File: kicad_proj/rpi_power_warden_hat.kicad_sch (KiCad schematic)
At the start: 4 parts, among them J1 54-00164, J2 54-00164, J3 54-00003

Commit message: checked all the schematics
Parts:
- TP1: now left out of the parts list
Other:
- moved on the sheet: J1, J2, J3, TP1

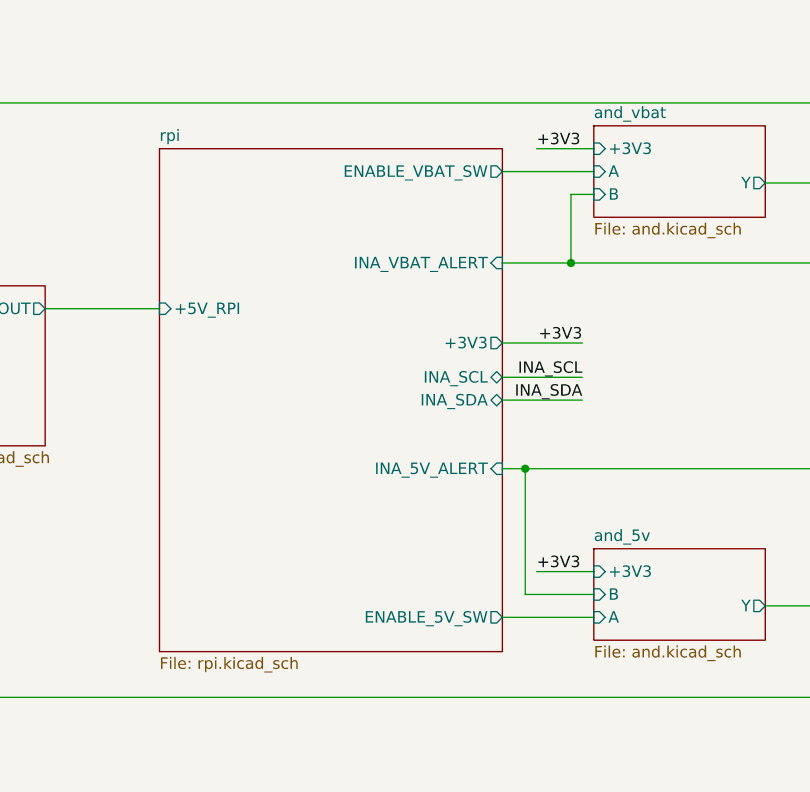
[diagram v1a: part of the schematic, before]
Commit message: run ERC and fix some errors (no critical errors, mostly associated to raspberry pi connectors not connected and with not NC flag
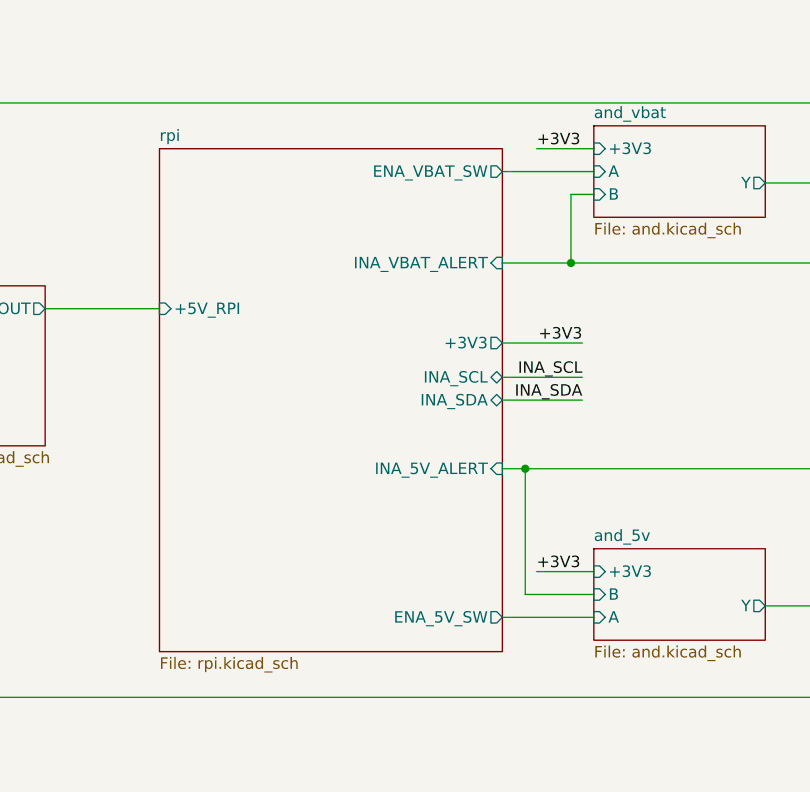
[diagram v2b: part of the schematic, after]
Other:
- sheet rpi ports: added ENA_5V_SW, ENA_VBAT_SW; removed ENABLE_5V_SW, ENABLE_VBAT_SW
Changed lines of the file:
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@@
 			)
 		)
-		(pin "ENABLE_5V_SW" output
+		(pin "ENA_5V_SW" output
 			(at 130.81 115.57 0)
 			(effects
@@
 			)
 		)
-		(pin "ENABLE_VBAT_SW" output
+		(pin "ENA_VBAT_SW" output
 			(at 130.81 66.04 0)
 			(effects

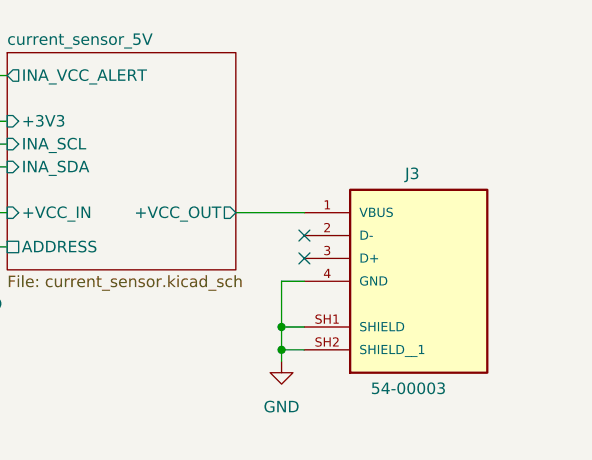
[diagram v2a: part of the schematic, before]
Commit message: changed usb A for an usb C with more stock
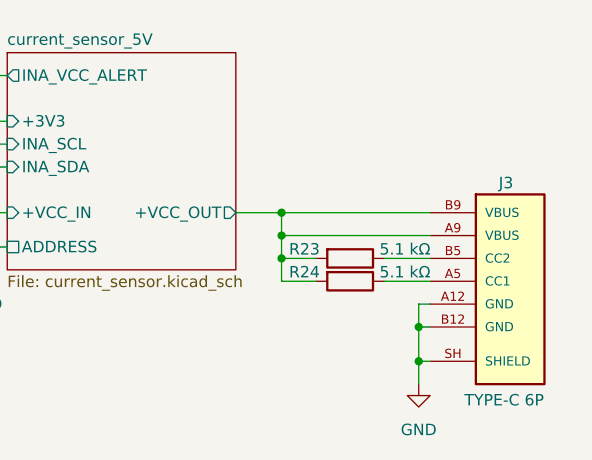
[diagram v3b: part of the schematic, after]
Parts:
- removed J3: 54-00003, rpi_power_warden_hat:TENSILITY_54-00003, symbol rpi_power_warden_hat:54-00003
- added J3: TYPE-C 6P, rpi_power_warden_hat:SHOU_HAN_TYPE-C-6P, symbol rpi_power_warden_hat:SHOU-HAN-TYPE-C-6P
- added R23, R24: 5.1 kΩ, Resistor_SMD:R_0603_1608Metric_Pad0.98x0.95mm_HandSolder, symbol Device:R
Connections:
- net GND: now also J3.A12 (GND), J3.B12 (GND), J3.SH (SHIELD)
- net current_sensor_5V/+VCC_OUT: now also J3.A9 (VBUS), J3.B9 (VBUS), R23.2, R24.2
- new net: J3.A5 (CC1), R24.1
- new net: J3.B5 (CC2), R23.1
- no-connect marks 2 -> 0

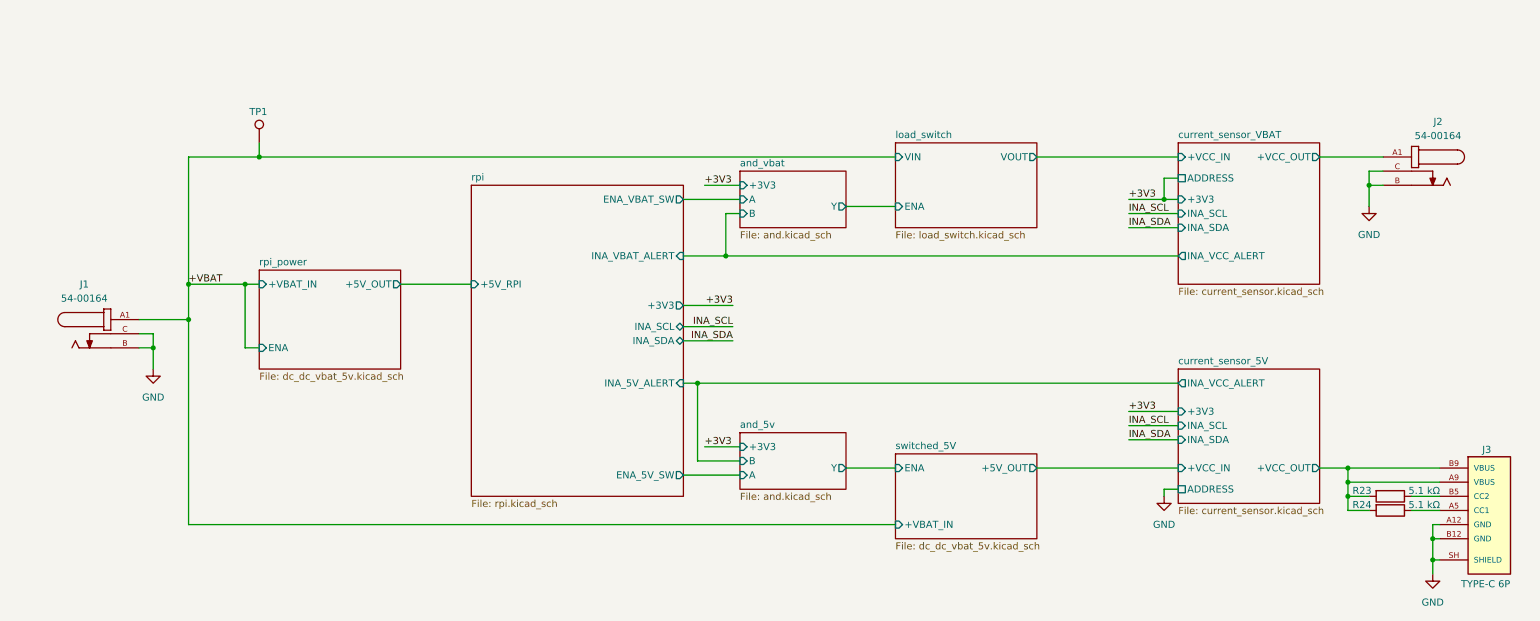
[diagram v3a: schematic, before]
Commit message: replace DC jack for one with stock
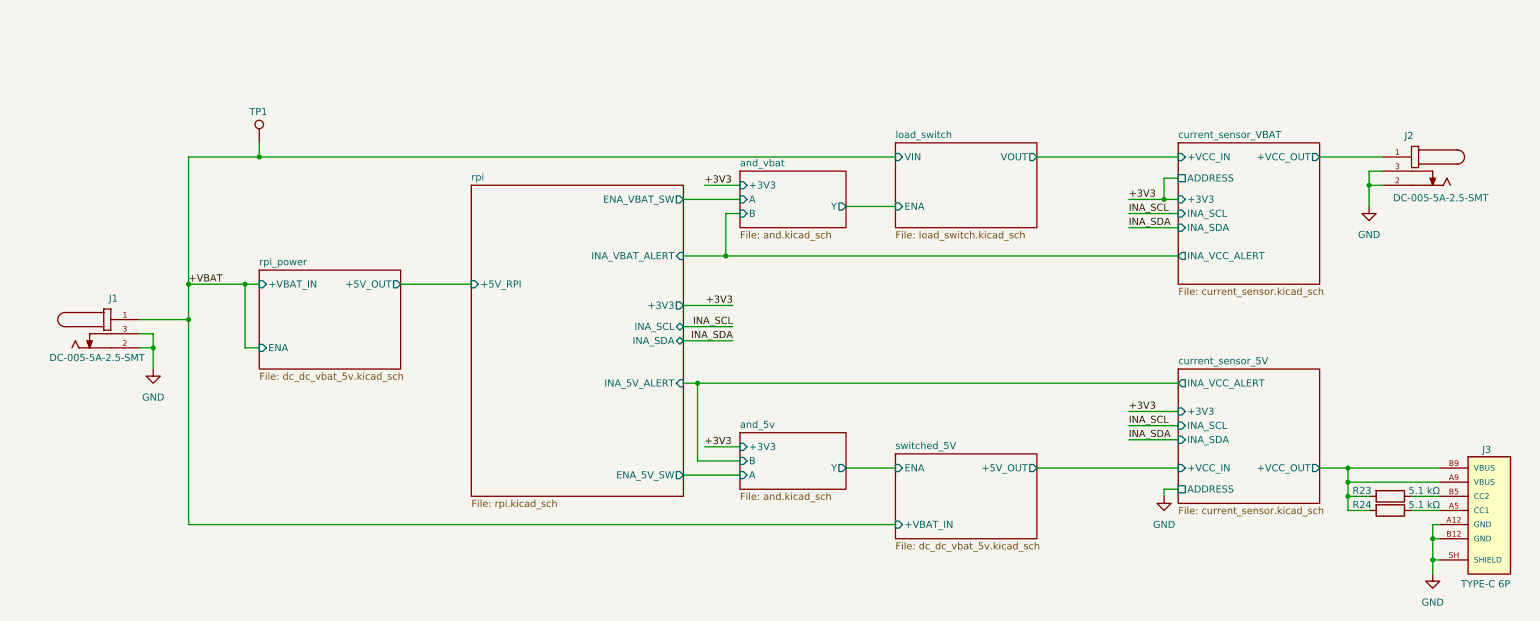
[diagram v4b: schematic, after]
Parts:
- removed J1, J2: 54-00164, rpi_power_warden_hat:TENSILITY_54-00164, symbol rpi_power_warden_hat:54-00164
- added J1, J2: DC-005-5A-2.5-SMT, rpi_power_warden_hat:XKB_DC-005-5A-2.5-SMT, symbol rpi_power_warden_hat:DC-005-5A-2.5-SMT
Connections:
- net +VBAT: now also J1.1, J1.A2
- net GND: now also J1.2, J1.3, J2.2, J2.3
- net current_sensor_VBAT/+VCC_OUT: now also J2.1, J2.A2
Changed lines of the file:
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@@
+	)
+	(symbol
+		(lib_id "rpi_power_warden_hat:DC-005-5A-2.5-SMT")
+		(at 261.62 60.96 0)
+		(mirror y)
+		(unit 1)
+		(exclude_from_sim no)
+		(in_bom yes)
+		(on_board yes)
+		(dnp no)
+		(property "Reference" "J2"
+			(at 260.35 54.61 0)
+			(effects
+				(font
+					(size 1.27 1.27)
+				)
+				(justify right)
+			)
+		)
+		(property "Value" "DC-005-5A-2.5-SMT"
+			(at 258.318 65.786 0)
+			(effects
+				(font
+					(size 1.27 1.27)
+				)
+				(justify right)
+			)
+		)
+		(property "Footprint" "rpi_power_warden_hat:XKB_DC-005-5A-2.5-SMT"
+			(at 258.572 48.006 0)
+			(effects
+				(font
+					(size 1.27 1.27)
+				)
+				(justify bottom)
+				(hide yes)
+			)
+		)
+		(property "Datasheet" "https://lcsc.com/datasheet/lcsc_datasheet_2404011025_XKB-Connection-DC-005-5A-2-5-SMT_C319133.pdf"
+			(at 258.572 48.006 0)
+			(effects
+				(font
+					(size 1.27 1.27)
+				)
+				(hide yes)
+			)
+		)
+		(property "Description" "Surface Mount, Right Angle DC Power Jack -20℃~+70℃ 2.5mm 6.5mm 5A 24V SMD DC Power Connectors ROHS"
+			(at 260.858 50.546 0)
+			(effects
+				(font
+					(size 1.27 1.27)
+				)
+				(hide yes)
+			)
+		)
+		(property "mpn" "DC-005-5A-2.5-SMT"
+			(at 262.636 52.832 0)
+			(effects
+				(font
+					(size 1.27 1.27)
+				)
+				(justify bottom)
+				(hide yes)
+			)
+		)
+		(property "manufacturer" "XKB Connection"
+			(at 260.604 52.324 0)
+			(effects
+				(font
+					(size 1.27 1.27)
+				)
+				(justify bottom)
+				(hide yes)
+			)
+		)
+		(pin "2"
+		)
+		(pin "A2"
+		)
+		(pin "3"
+		)
+		(pin "1"
+		)
+		(instances
+			(project ""
+				(path "/8692c5de-a943-41e8-8e29-f6c5e99cda34"
+					(reference "J2")
+					(unit 1)
+				)
+			)
+		)
 	)
 	(symbol
@@
 	)
 	(symbol
-		(lib_id "rpi_power_warden_hat:54-00164")
-		(at 261.62 60.96 0)
-		(mirror y)
-		(unit 1)
-		(exclude_from_sim no)
-		(in_bom yes)
-		(on_board yes)
-		(dnp no)
-		(property "Reference" "J2"
-			(at 266.3797 52.07 0)
-			(effects
-				(font
-					(size 1.27 1.27)
-				)
-			)
-		)
-		(property "Value" "54-00164"
-			(at 266.3797 54.61 0)
-			(effects
-				(font
-					(size 1.27 1.27)
-				)
-			)
-		)
-		(property "Footprint" "rpi_power_warden_hat:TENSILITY_54-00164"
-			(at 258.572 48.006 0)
-			(effects
-				(font
-					(size 1.27 1.27)
-				)
-				(justify bottom)
-				(hide yes)
-			)
-		)
-		(property "Datasheet" "https://tensility.s3.us-west-2.amazonaws.com/uploads/pdffiles/54-00164.pdf"
-			(at 258.572 48.006 0)
-			(effects
-				(font
-					(size 1.27 1.27)
-				)
-				(hide yes)
-			)
-		)
-		(property "Description" "CONN JACK R/A SMT 5.5X2.1MM"
-			(at 260.858 50.546 0)
-			(effects
-				(font
-					(size 1.27 1.27)
-				)
-				(hide yes)
-			)
-		)
-		(property "mpn" "54-00164"
-			(at 262.636 52.832 0)
-			(effects
-				(font
-					(size 1.27 1.27)
-				)
-				(justify bottom)
-				(hide yes)
-			)
-		)
-		(property "manufacturer" "TENSILITY"
-			(at 260.604 52.324 0)
-			(effects
-				(font
-					(size 1.27 1.27)
-				)
-				(justify bottom)
-				(hide yes)
-			)
-		)
-		(pin "A2"
-		)
-		(pin "B"
-		)
-		(pin "C"
-		)
-		(pin "A1"
-		)
-		(instances
-			(project "rpi_power_warden_hat"
-				(path "/8692c5de-a943-41e8-8e29-f6c5e99cda34"
-					(reference "J2")
-					(unit 1)
-				)
-			)
-		)
-	)
-	(symbol
 		(lib_id "Device:R")
 		(at 257.81 119.38 270)
@@
 				(path "/8692c5de-a943-41e8-8e29-f6c5e99cda34"
 					(reference "R23")
+					(unit 1)
+				)
+			)
+		)
+	)
+	(symbol
+		(lib_id "rpi_power_warden_hat:DC-005-5A-2.5-SMT")
+		(at 27.94 90.17 0)
+		(unit 1)
+		(exclude_from_sim no)
+		(in_bom yes)
+		(on_board yes)
+		(dnp no)
+		(property "Reference" "J1"
+			(at 29.21 83.82 0)
+			(effects
+				(font
+					(size 1.27 1.27)
+				)
+				(justify right)
+			)
+		)
+		(property "Value" "DC-005-5A-2.5-SMT"
+			(at 34.036 94.488 0)
+			(effects
+				(font
+					(size 1.27 1.27)
+				)
+				(justify right)
+			)
+		)
+		(property "Footprint" "rpi_power_warden_hat:XKB_DC-005-5A-2.5-SMT"
+			(at 30.988 77.216 0)
+			(effects
+				(font
+					(size 1.27 1.27)
+				)
+				(justify bottom)
+				(hide yes)
+			)
+		)
+		(property "Datasheet" "https://lcsc.com/datasheet/lcsc_datasheet_2404011025_XKB-Connection-DC-005-5A-2-5-SMT_C319133.pdf"
+			(at 30.988 77.216 0)
+			(effects
+				(font
+					(size 1.27 1.27)
+				)
+				(hide yes)
+			)
+		)
+		(property "Description" "Surface Mount, Right Angle DC Power Jack -20℃~+70℃ 2.5mm 6.5mm 5A 24V SMD DC Power Connectors ROHS"
+			(at 28.702 79.756 0)
+			(effects
+				(font
+					(size 1.27 1.27)
+				)
+				(hide yes)
+			)
+		)
+		(property "mpn" "DC-005-5A-2.5-SMT"
+			(at 26.924 82.042 0)
+			(effects
+				(font
+					(size 1.27 1.27)
+				)
+				(justify bottom)
+				(hide yes)
+			)
+		)
+		(property "manufacturer" "XKB Connection"
+			(at 28.956 81.534 0)
+			(effects
+				(font
+					(size 1.27 1.27)
+				)
+				(justify bottom)
+				(hide yes)
+			)
+		)
+		(pin "2"
+		)
+		(pin "A2"
+		)
+		(pin "3"
+		)
+		(pin "1"
+		)
+		(instances
+			(project "rpi_power_warden_hat"
+				(path "/8692c5de-a943-41e8-8e29-f6c5e99cda34"
+					(reference "J1")
 					(unit 1)
 				)
@@
 					(unit 1)
 				)
-			)
-		)
-	)
-	(symbol
-		(lib_id "rpi_power_warden_hat:54-00164")
-		(at 27.94 90.17 0)
-		(unit 1)
-		(exclude_from_sim no)
-		(in_bom yes)
-		(on_board yes)
-		(dnp no)
-		(fields_autoplaced yes)
-		(property "Reference" "J1"
-			(at 23.1803 81.28 0)
-			(effects
-				(font
-					(size 1.27 1.27)
-				)
-			)
-		)
-		(property "Value" "54-00164"
-			(at 23.1803 83.82 0)
-			(effects
-				(font
-					(size 1.27 1.27)
-				)
-			)
-		)
-		(property "Footprint" "rpi_power_warden_hat:TENSILITY_54-00164"
-			(at 30.988 77.216 0)
-			(effects
-				(font
-					(size 1.27 1.27)
-				)
-				(justify bottom)
-				(hide yes)
-			)
-		)
-		(property "Datasheet" "https://tensility.s3.us-west-2.amazonaws.com/uploads/pdffiles/54-00164.pdf"
-			(at 30.988 77.216 0)
-			(effects
-				(font
-					(size 1.27 1.27)
-				)
-				(hide yes)
-			)
-		)
-		(property "Description" "CONN JACK R/A SMT 5.5X2.1MM"
-			(at 28.702 79.756 0)
-			(effects
-				(font
-					(size 1.27 1.27)
-				)
-				(hide yes)
-			)
-		)
-		(property "mpn" "54-00164"
-			(at 26.924 82.042 0)
-			(effects
-				(font
-					(size 1.27 1.27)
-				)
-				(justify bottom)
-				(hide yes)
-			)
-		)
-		(property "manufacturer" "TENSILITY"
-			(at 28.956 81.534 0)
-			(effects
-				(font
-					(size 1.27 1.27)
-				)
-				(justify bottom)
-				(hide yes)
-			)
-		)
-		(pin "A2"
-		)
-		(pin "B"
-		)
-		(pin "C"
-		)
-		(pin "A1"
-		)
-		(instances
-			(project "rpi_power_warden_hat"
-				(path "/8692c5de-a943-41e8-8e29-f6c5e99cda34"
-					(reference "J1")
-					(unit 1)
-				)
